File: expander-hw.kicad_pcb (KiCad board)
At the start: 2 copper layers, 44.2 x 22.6 mm, 29 parts, among them J1 Conn_ARM_SWD_TagConnect_TC203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, J2 USB_C_Receptacle_USB2.0_16P, J3 Conn_02x08_Odd_Even, U1 STM32H523RETx, U2 USBLC6-2SC6, U3 AZ1117-3.3, U4 SRDA3.3-4BTG, U5 SRDA3.3-4BTG, U6 SRDA3.3-4BTG

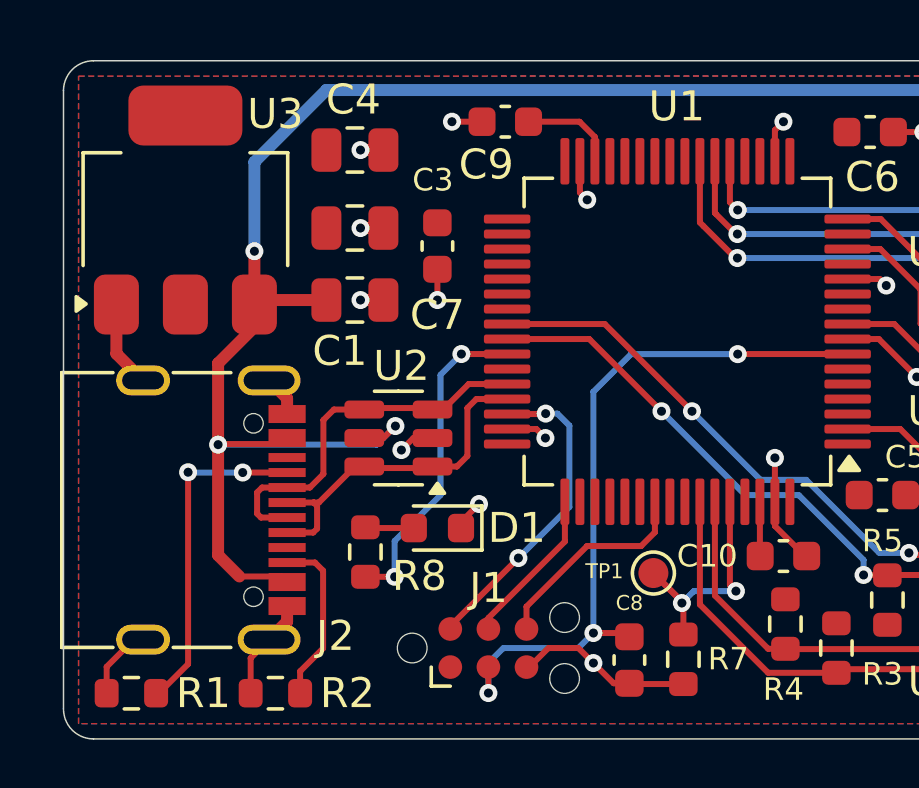
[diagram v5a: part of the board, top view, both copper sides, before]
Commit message: Move boot pin to back and add tear drops
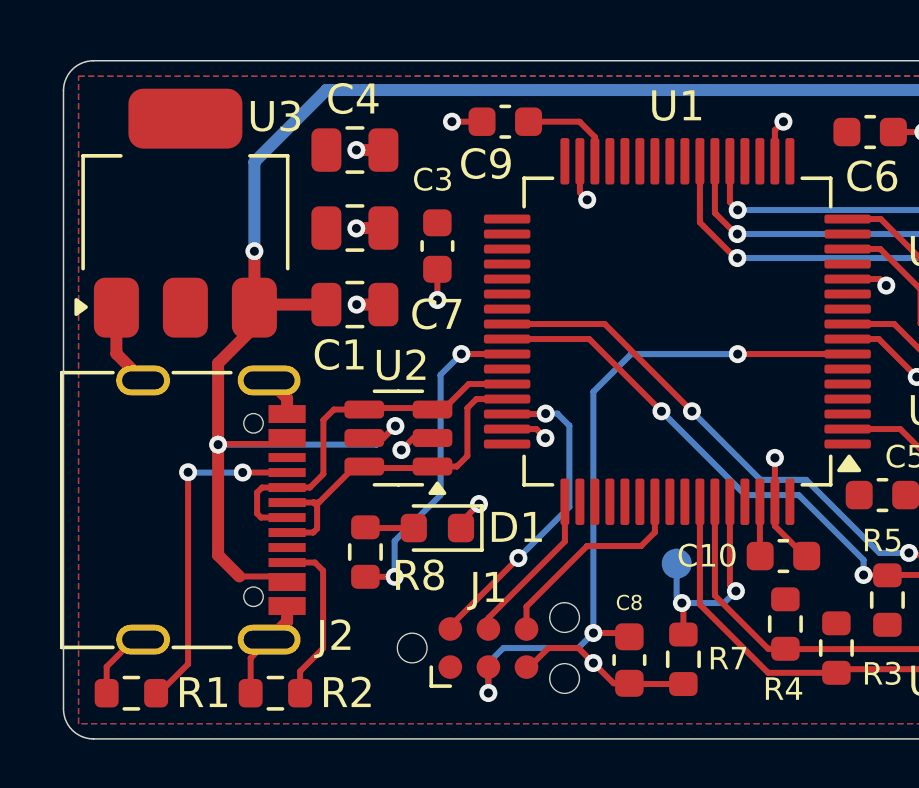
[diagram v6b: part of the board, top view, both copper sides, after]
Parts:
- TP1: moved to B.Cu
- moved TP1 0.84 mm to (128.8, 107.2), turned to 180 degrees
- moved C1 0.15 mm to (118.0, 98.6)
- moved U3 0.10 mm to (112.4, 95.5)
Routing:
- net /BOOT0: track 8.88 -> 7.63 mm

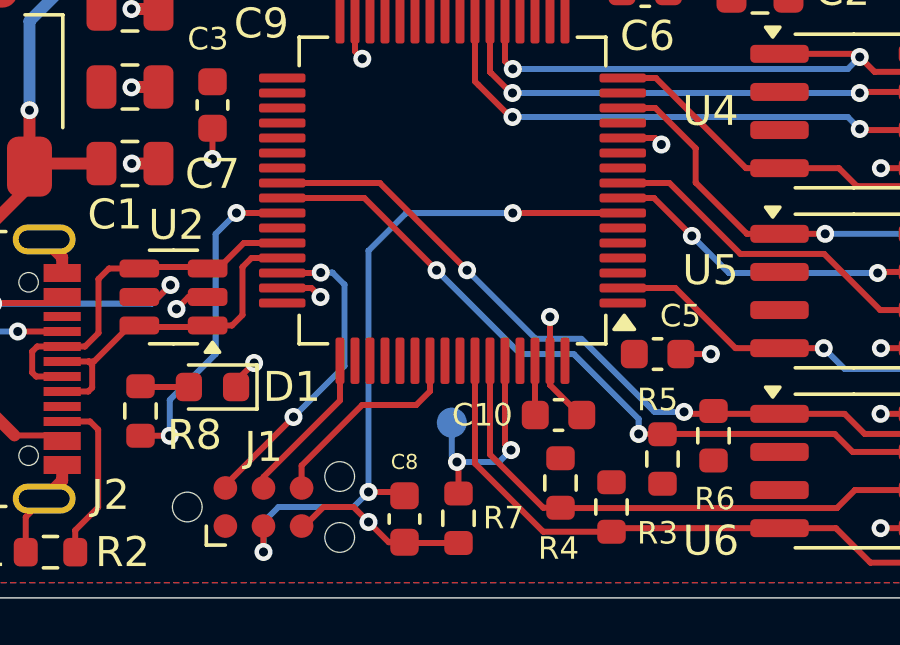
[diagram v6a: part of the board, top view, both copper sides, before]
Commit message: Increase boot pad size
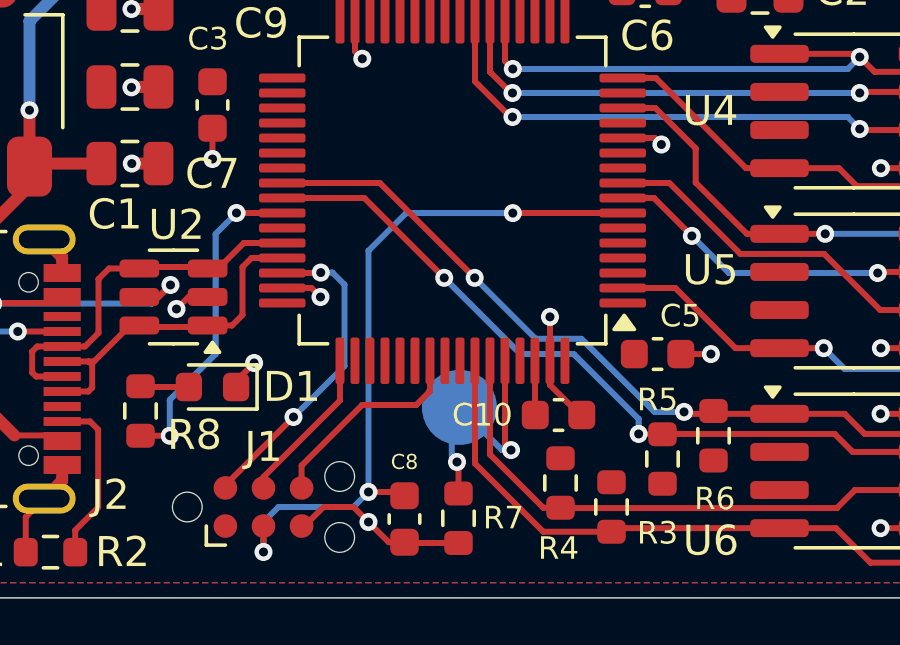
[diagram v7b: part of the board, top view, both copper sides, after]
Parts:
- removed TP1: BOOT, TestPoint:TestPoint_Pad_D1.0mm
- added BOOT: TestPoint_Pad_D2.5mm, TestPoint:TestPoint_Pad_D2.5mm, B.Cu at (129.0, 106.7)
